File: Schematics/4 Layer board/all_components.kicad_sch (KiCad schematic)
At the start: 78 parts, among them J2 Conn_01x01, J3 5V-Relay, J4 5V-Relay, J8 S08B-PUDSS-1LFSN, J9 3-pin-header, Q1 OPTOCOUPLER, Q2 OPTOCOUPLER, T1 PNP, T2 PNP, T3 PNP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

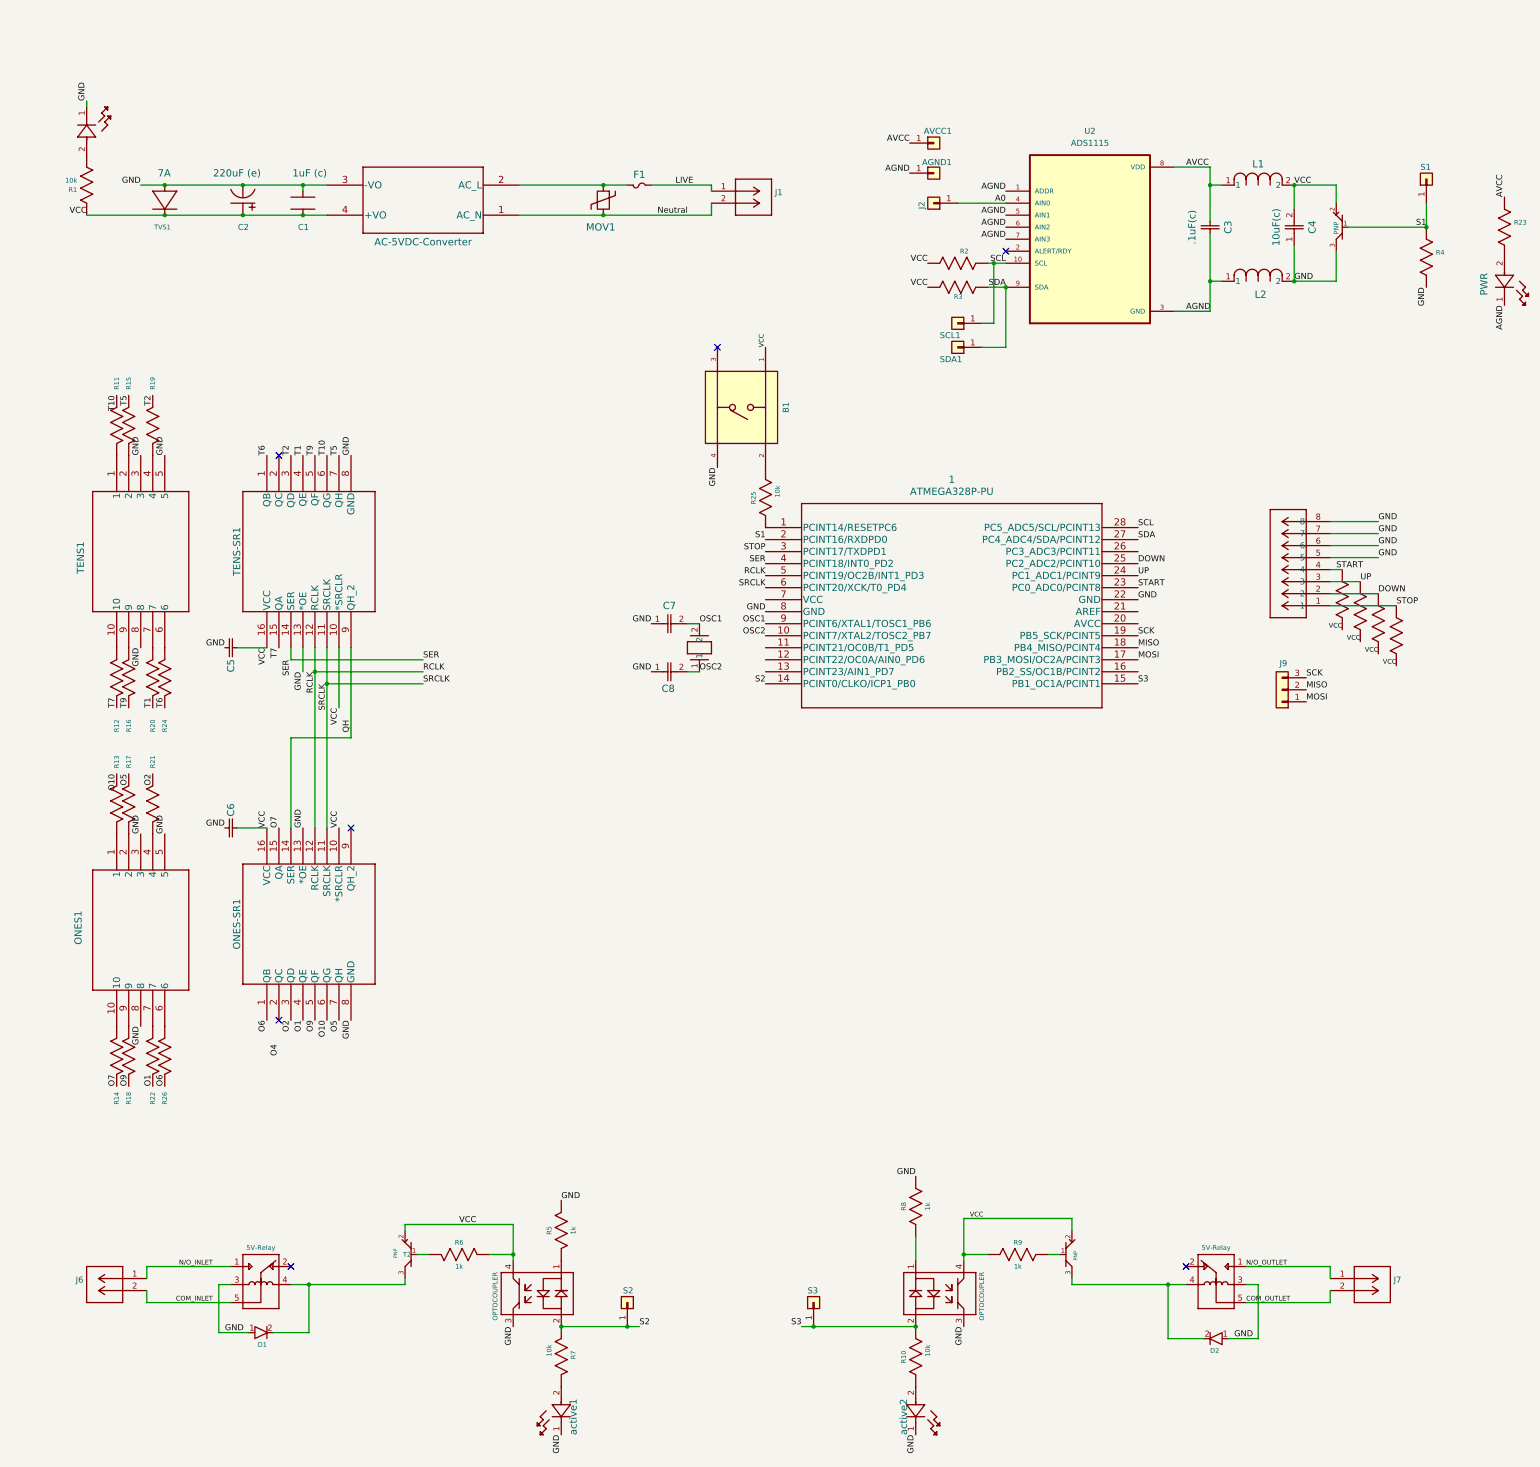
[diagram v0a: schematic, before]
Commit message: updated board and kicad lib
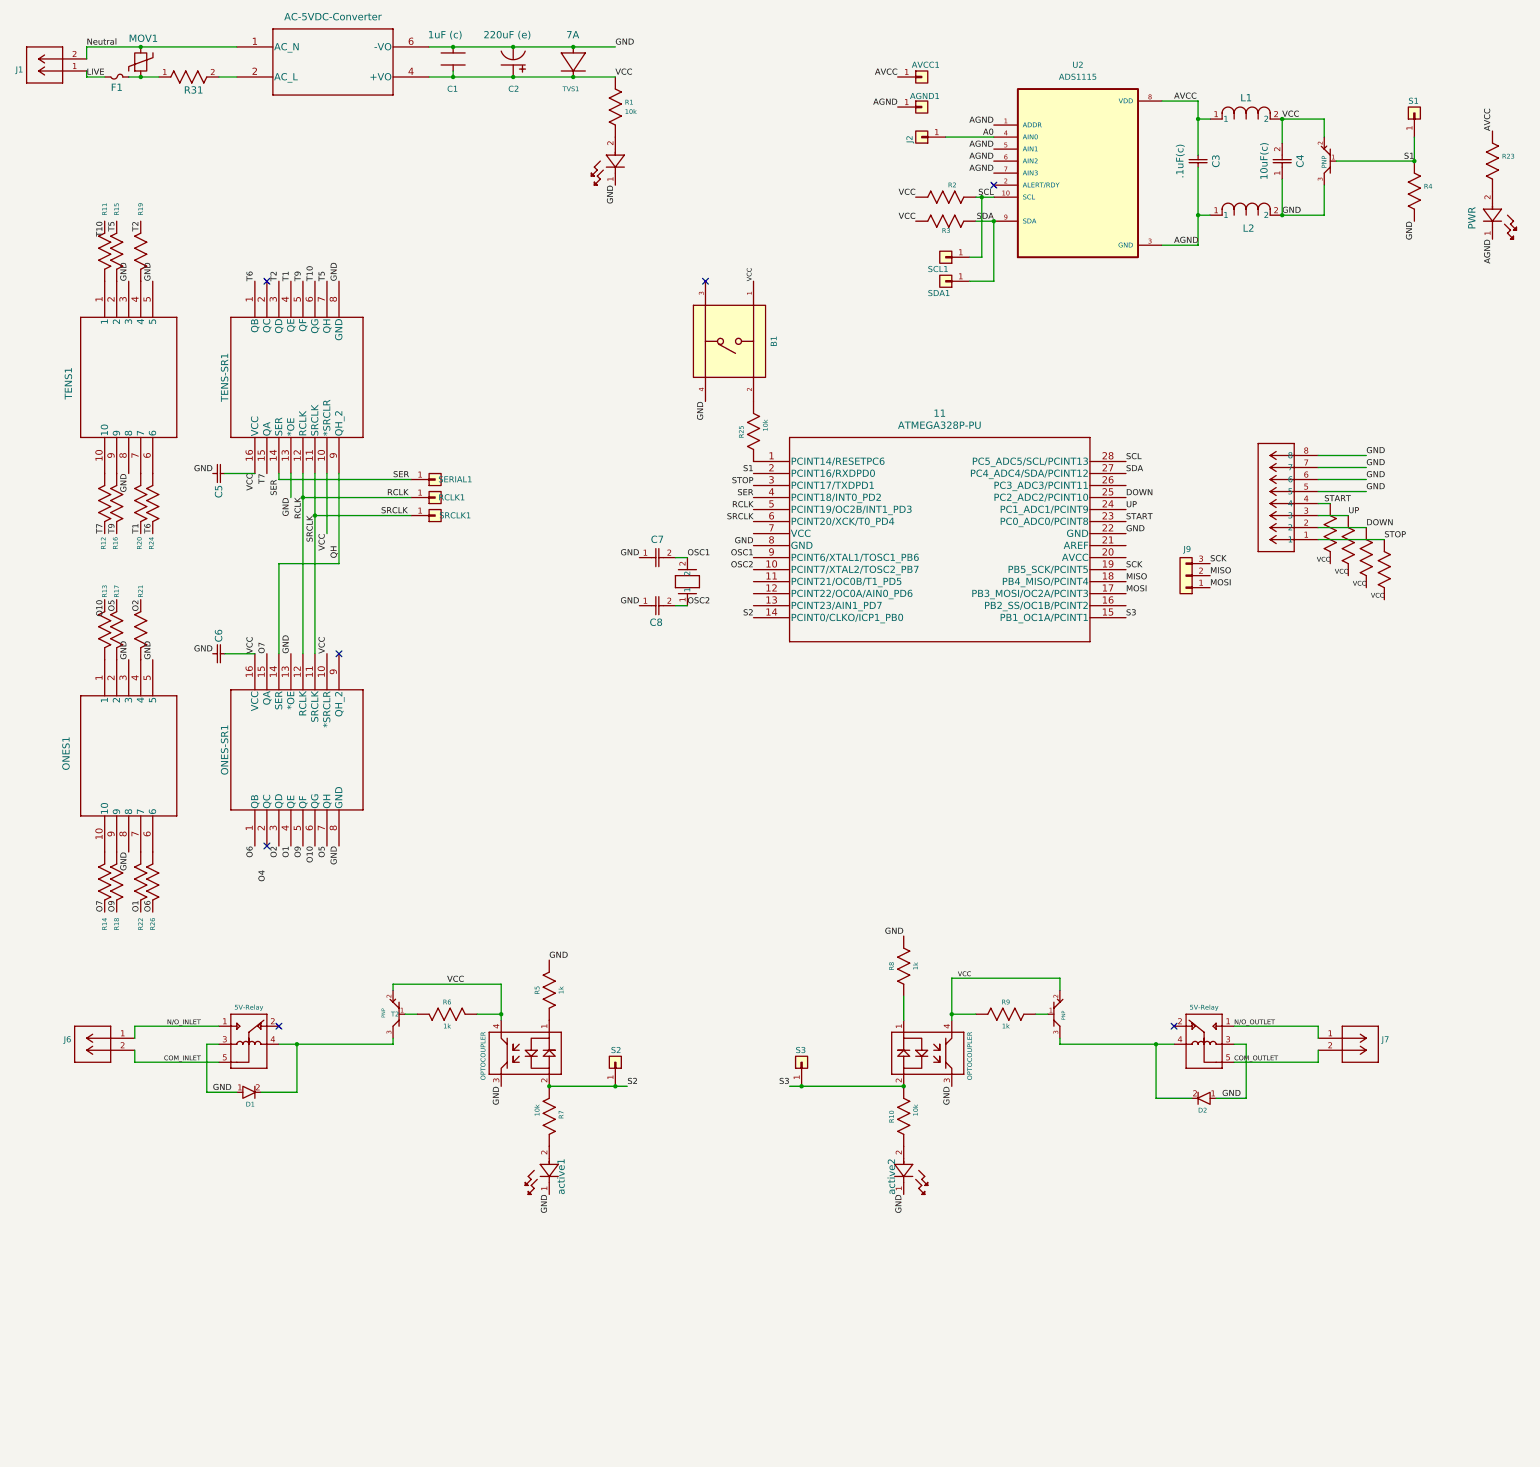
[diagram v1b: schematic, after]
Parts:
- removed u1: AC-5VDC-Converter, pPSI:ac-dc converter, symbol pPSI:AC-5VDC-Converter
- added R31: 6.8ohm, pPSI:6.8ohm, symbol pPSI:6.8ohm
- added RCLK1, SERIAL1, SRCLK1: Conn_01x01, pPSI:1 pin header, symbol Connector_Generic:Conn_01x01
- added u3: AC-5VDC-Converter, pPSI:CONV_PSK-10D-5, symbol pPSI:AC-5VDC-Converter
- C2: footprint pPSI:220uF electrolytic capacitor -> pPSI:220uF Cap (e)
- C3, C5, C6: footprint pPSI:.1uF ceramic capacitor -> pPSI:.1uF Cap (c)
- C4: footprint pPSI:10uF Ceramic Capacitor -> pPSI:10uF Cap (c)
- C7, C8: footprint pPSI:22pFCeramicCap -> pPSI:22pF Cap (c)
- F1: footprint pPSI:FUSE -> pPSI:Fuse
- MOV1: value 470V-Varistor -> ~; footprint pPSI:470V Varistor -> pPSI:350V_4.5kA MOV
- R1, R10, R2, R23, R25, R3, R4, R7: footprint pPSI:10kohm resistor -> pPSI:10kohm
- R11, R12, R13, R14, R15, R16, R17, R18, R19, R20, R21, R22, R24, R26: footprint pPSI:100ohm resistor -> pPSI:100ohm
- R27, R28, R29, R30, R5, R6, R8, R9: footprint pPSI:1kohm resistor -> pPSI:1kohm
- renumbered 1 to 11
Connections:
- net GND: now also C1.2, u3.6 (-VO); no longer C1.1
- net Neutral: now also u3.1 (AC_N)
- net RCLK: now also RCLK1.1 (Pin_1)
- net SER: now also SERIAL1.1 (Pin_1)
- net SRCLK: now also SRCLK1.1 (Pin_1)
- net VCC: now also C1.1, u3.4 (+VO); no longer C1.2
- net at F1.1, MOV1.2: now also R31.1
- new net: R31.2, u3.2 (AC_L)
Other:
- moved on the sheet: 11, AGND1, AVCC1, B1, C1, C2, C3, C4, C5, C6, C7, C8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

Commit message: updated board for AC optimization
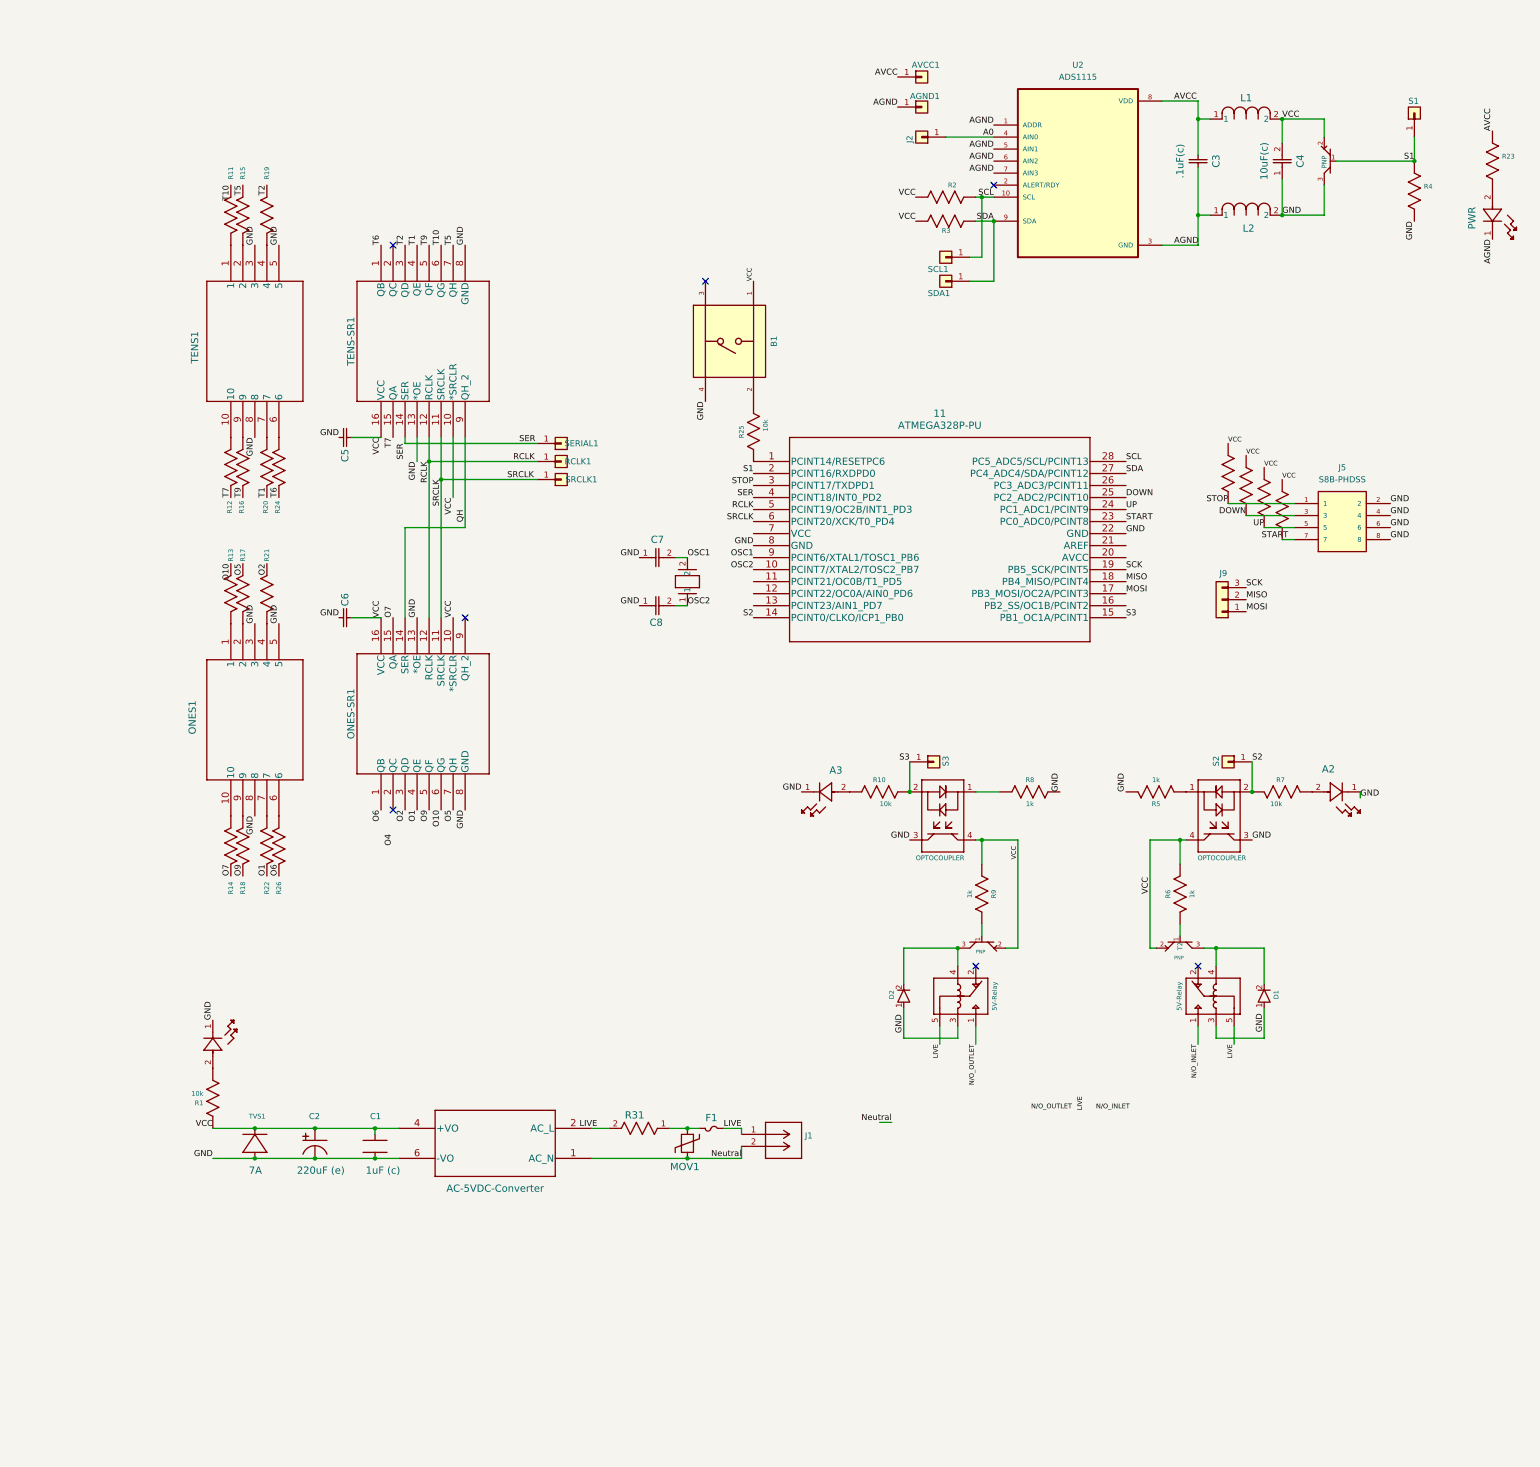
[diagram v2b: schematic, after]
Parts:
- removed J6, J7: ~, pPSI:2 pin header, symbol pPSI:2-pin-terminal-block
- removed J8: S08B-PUDSS-1LFSN, pPSI:2x4Connector, symbol pPSI:S08B-PUDSS-1LFSN
- added J5: S8B-PHDSS, pPSI:2x4 female connector, symbol pPSI:S8B-PHDSS
- renumbered active1 to A2, active2 to A3
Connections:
- net COM_INLET is gone; now on net LIVE: J3.5
- net COM_OUTLET is gone; now on net LIVE: J4.5
- net DOWN: now also J5.3
- net GND: now also J5.2, J5.4, J5.6, J5.8
- net LIVE: now also R31.2, u3.2 (AC_L)
- net START: now also J5.7
- net STOP: now also J5.1
- net UP: now also J5.5
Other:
- moved on the sheet: A2, A3, C1, C2, C5, C6, D1, D2, F1, J1, J9, MOV1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

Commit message: more CAD files and updated layout
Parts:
- added S4, S5, S6, S7: Conn_01x01, pPSI:1 pin header, symbol Connector_Generic:Conn_01x01
- C2: footprint pPSI:220uF Cap (e) -> pPSI:220uF (e)
- C8: value C0805C220J5GAC7210 -> (none)
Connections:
- net Neutral: now also S6.1 (Pin_1), S7.1 (Pin_1)
- net N/O_INLET: now also S4.1 (Pin_1)
- net N/O_OUTLET: now also S5.1 (Pin_1)

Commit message: updated cad files
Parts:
- removed AGND1, AVCC1, J2, S4, S5, S6, S7: Conn_01x01, pPSI:1 pin header, symbol Connector_Generic:Conn_01x01
- removed J1: ~, pPSI:2 pin header, symbol pPSI:2-pin-terminal-block
- added J1, J2, J7: OSTTF020161, pPSI:1x2 terminal block, symbol pPSI:OSTTF020161
- added J6: OSTVN03A150, pPSI:1x3 terminal block, symbol pPSI:OSTVN03A150
- C8: value (none) -> ~
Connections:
- net A0: now also J6.2
- net AGND: now also J6.1
- net AVCC: now also J6.3
- net DOWN: now also J5.5, R29.2; no longer J5.3, R28.2
- net LIVE: now also J1.2
- net Neutral: now also J1.1, J2.1, J2.2
- net N/O_INLET: now also J7.2
- net N/O_OUTLET: now also J7.1
- net START: now also J5.1, R27.2; no longer J5.7, R30.2
- net STOP: now also J5.7, R30.2; no longer J5.1, R27.2
- net UP: now also J5.3, R28.2; no longer J5.5, R29.2
